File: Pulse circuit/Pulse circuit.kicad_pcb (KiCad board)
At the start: 2 copper layers, 4 parts, among them U1 ESP32-DevKitC, U2 module_max30102, U3 module_max30102

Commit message: Updated with relative path
🎯
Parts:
- U1: value ESP32-DevKitC -> module_max30102; footprint PCM_Espressif:ESP32-DevKitC -> usini_sensors:module_max30102
- U3: value module_max30102 -> DOIT-ESP32-DEVKIT-V1; footprint usini_sensors:module_max30102 -> doi-esp32-devkit:ESP32-DOIT-DEVKIT
- moved U3 65.5 mm to (239.4, 57.5)
- moved U1 54.7 mm to (132.7, 103.6)
- moved U2 42.9 mm to (149.7, 103.6)
- moved Brd1 24.2 mm to (79.6, 85.2)

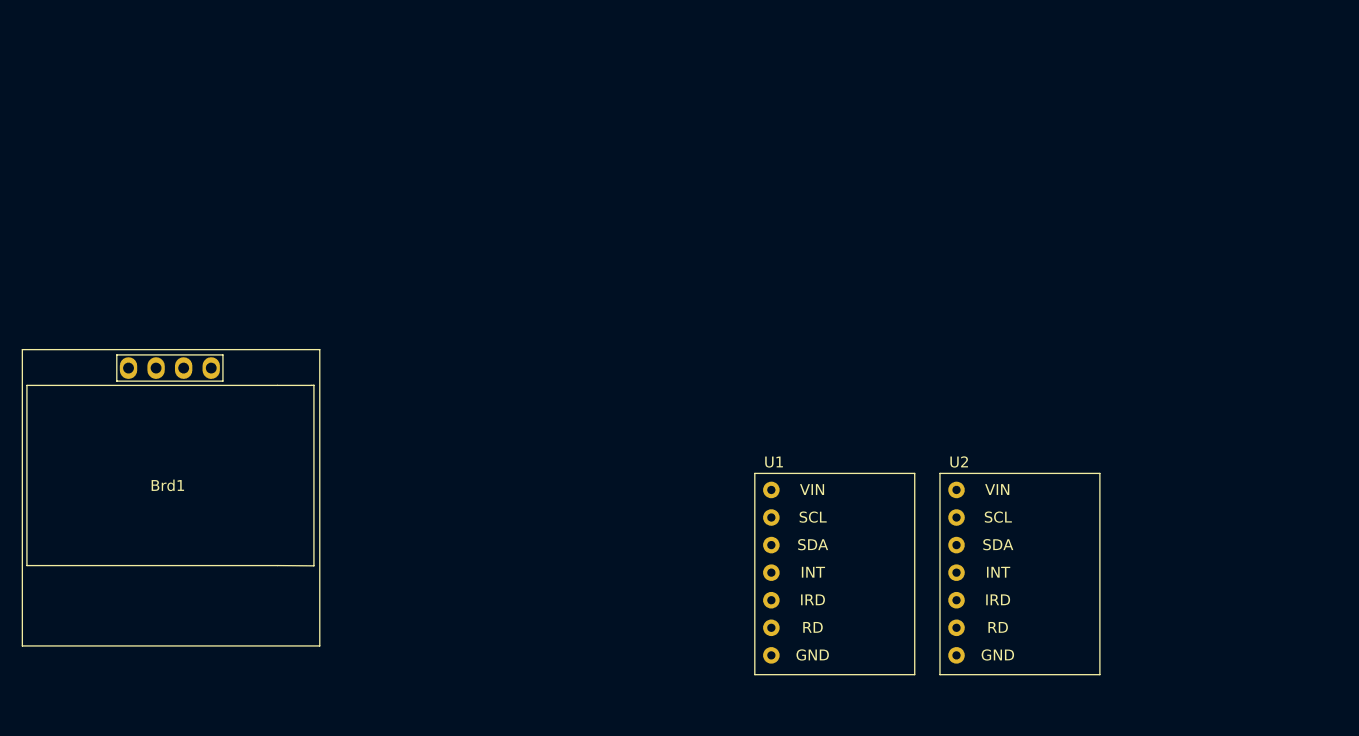
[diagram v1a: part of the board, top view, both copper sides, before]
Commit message: Changed footprint of the resistors
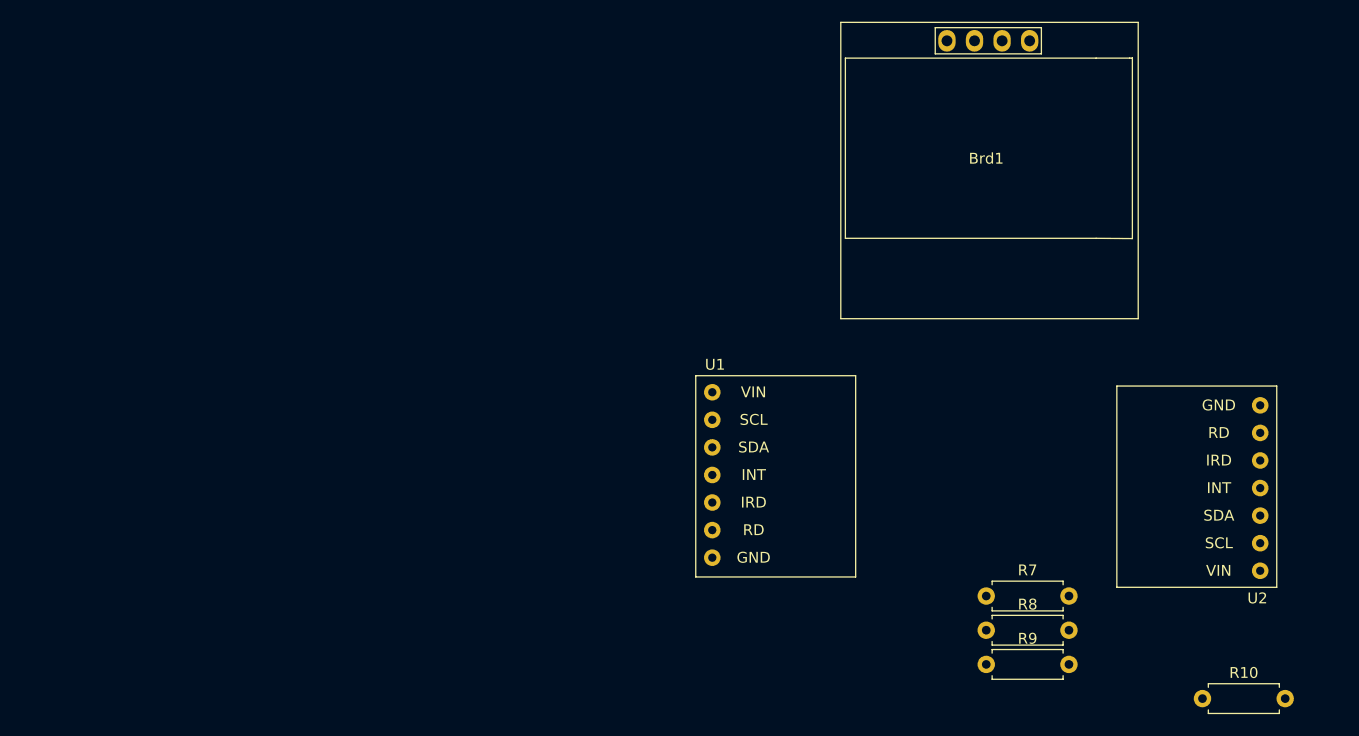
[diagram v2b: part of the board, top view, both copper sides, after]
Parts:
- added R10: 10k, Resistor_THT:R_Axial_DIN0207_L6.3mm_D2.5mm_P7.62mm_Horizontal, F.Cu at (174.9, 105.0)
- added R7: 10k, Resistor_THT:R_Axial_DIN0207_L6.3mm_D2.5mm_P7.62mm_Horizontal, F.Cu at (155.0, 95.5)
- added R8: 10k, Resistor_THT:R_Axial_DIN0207_L6.3mm_D2.5mm_P7.62mm_Horizontal, F.Cu at (155.0, 98.7)
- added R9: 10k, Resistor_THT:R_Axial_DIN0207_L6.3mm_D2.5mm_P7.62mm_Horizontal, F.Cu at (155.0, 101.8)
- moved Brd1 81.2 mm to (155.0, 55.0)
- moved U2 43.4 mm to (182.8, 75.4), turned to 180 degrees
- moved U1 10.5 mm to (127.2, 94.6)
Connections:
- Brd1 pad 1: unconnected-(Brd1-GND-Pad1) -> GND
- Brd1 pad 2: unconnected-(Brd1-VCC-Pad2) -> SDA
- Brd1 pad 3: unconnected-(Brd1-SCL-Pad3) -> SCL
- Brd1 pad 4: unconnected-(Brd1-SDA-Pad4) -> 3V3
- U1 pad 1: unconnected-(U1-VIN-Pad1) -> 3V3
- U1 pad 2: unconnected-(U1-SCL-Pad2) -> SCL
- U1 pad 3: unconnected-(U1-SDA-Pad3) -> SDA
- U1 pad 7: unconnected-(U1-GND-Pad7) -> GND
- U2 pad 1: unconnected-(U2-VIN-Pad1) -> 5V
- U2 pad 2: unconnected-(U2-SCL-Pad2) -> SCL
- U2 pad 3: unconnected-(U2-SDA-Pad3) -> SDA
- U2 pad 7: unconnected-(U2-GND-Pad7) -> GND
- U3 pad 18: unconnected-(U3-VIN-Pad18) -> 5V
- U3 pad 19: unconnected-(U3-3V3-Pad19) -> 3V3
- U3 pad 32: unconnected-(U3-GPIO21_I2C-SDA-Pad32) -> SDA
- U3 pad 35: unconnected-(U3-GPIO22_I2C-SCL-Pad35) -> SCL

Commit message: PCB 1/2
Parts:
- removed R10, R9: 10k, Resistor_THT:R_Axial_DIN0207_L6.3mm_D2.5mm_P7.62mm_Horizontal
- added R11: 10k, Resistor_THT:R_Axial_DIN0207_L6.3mm_D2.5mm_P7.62mm_Horizontal, F.Cu at (128.4, 69.3)
- added R12: 10k, Resistor_THT:R_Axial_DIN0207_L6.3mm_D2.5mm_P7.62mm_Horizontal, F.Cu at (132.4, 69.3)
- U1: moved to B.Cu
- moved U3 89.7 mm to (151.9, 77.3)
- moved R8 39.6 mm to (176.7, 65.6), turned to 180 degrees
- moved R7 33.9 mm to (176.7, 69.5), turned to 180 degrees
- moved U1 31.8 mm to (152.0, 74.7), turned to 180 degrees
- moved U2 23.0 mm to (166.6, 59.1)
- moved Brd1 5.99 mm to (151.8, 60.0)
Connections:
- U1 pad 1: 3V3 -> GND
- U1 pad 4: unconnected-(U1-INT-Pad4) -> 3V3
- U1 pad 5: unconnected-(U1-IRD-Pad5) -> GND
- U1 pad 6: unconnected-(U1-RD-Pad6) -> RD3v3
- U1 pad 7: GND -> IRD3v3
- U2 pad 4: unconnected-(U2-INT-Pad4) -> GND
- U2 pad 5: unconnected-(U2-IRD-Pad5) -> INT5v
- U2 pad 6: unconnected-(U2-RD-Pad6) -> IRD5v
- U2 pad 7: GND -> RD5v
- U3 pad 4: unconnected-(U3-GPIO34_ADC1-CH6_RTC-GPIO4-Pad4) -> RD3v3
- U3 pad 5: unconnected-(U3-GPIO35_ADC1-CH7_RTC-GPIO5-Pad5) -> IRD3v3
- U3 pad 6: unconnected-(U3-GPIO32_ADC1-CH4_RTC-GPIO9-Pad6) -> INT3v3
- U3 pad 7: unconnected-(U3-GPIO33_ADC1-CH5_RTC-GPIO8-Pad7) -> INT5v
- U3 pad 8: unconnected-(U3-GPIO25_ADC2-CH8_DAC1_RTC-GPIO6-Pad8) -> RD5v
- U3 pad 9: unconnected-(U3-GPIO26_ADC2-CH9_DAC2_RTC-GPIO7-Pad9) -> IRD5v
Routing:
- net SCL: track 0.00 -> 128.3 mm
- net SDA: track 0.00 -> 108.7 mm
- net IRD5v: track 0.00 -> 53.1 mm
- net RD5v: track 0.00 -> 42.0 mm
- net RD3v3: track 0.00 -> 31.3 mm
- net IRD3v3: track 0.00 -> 28.9 mm
- net INT3v3: track 0.00 -> 27.2 mm
- net INT5v: track 0.00 -> 18.1 mm
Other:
- copper layers 2 -> 4

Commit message: Added the GND plane
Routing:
- net GND: vias 0 -> 4
- added copper zone on In2.Cu, net GND
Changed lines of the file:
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@@
 			(layer "F.SilkS")
+		)
+		(fp_text user "GND"
+			(at 9.775 -10.03 0)
+			(layer "B.SilkS")
+			(effects
+				(font
+					(size 1 1)
+					(thickness 0.15)
+				)
+				(justify mirror)
+			)
 		)
 		(fp_text user "SCL"
@@
 			)
 		)
-		(fp_text user "GND"
-			(at 9.775 -10.03 0)
+		(fp_text user "RD"
+			(at 9.775 -7.49 0)
+			(layer "B.SilkS")
+			(effects
+				(font
+					(size 1 1)
+					(thickness 0.15)
+				)
+				(justify mirror)
+			)
+		)
+		(fp_text user "SDA"
+			(at 5.65 -7.515 0)
+			(layer "B.SilkS")
+			(effects
+				(font
+					(size 1 1)
+					(thickness 0.15)
+				)
+				(justify mirror)
+			)
+		)
+		(fp_text user "IRD"
+			(at 9.775 -4.95 0)
+			(layer "B.SilkS")
+			(effects
+				(font
+					(size 1 1)
+					(thickness 0.15)
+				)
+				(justify mirror)
+			)
+		)
+		(fp_text user "VIN"
+			(at 5.65 -10.055 0)
 			(layer "B.SilkS")
 			(effects
@@
 		(fp_text user "INT"
 			(at 9.775 -2.41 0)
-			(layer "B.SilkS")
-			(effects
-				(font
-					(size 1 1)
-					(thickness 0.15)
-				)
-				(justify mirror)
-			)
-		)
-		(fp_text user "RD"
-			(at 9.775 -7.49 0)
-			(layer "B.SilkS")
-			(effects
-				(font
-					(size 1 1)
-					(thickness 0.15)
-				)
-				(justify mirror)
-			)
-		)
-		(fp_text user "SDA"
-			(at 5.65 -7.515 0)
-			(layer "B.SilkS")
-			(effects
-				(font
-					(size 1 1)
-					(thickness 0.15)
-				)
-				(justify mirror)
-			)
-		)
-		(fp_text user "IRD"
-			(at 9.775 -4.95 0)
-			(layer "B.SilkS")
-			(effects
-				(font
-					(size 1 1)
-					(thickness 0.15)
-				)
-				(justify mirror)
-			)
-		)
-		(fp_text user "VIN"
-			(at 5.65 -10.055 0)
 			(layer "B.SilkS")
 			(effects
@@
 		(net 3)
 	)
+	(via
+		(at 138.344606 69.1675)
+		(size 0.6)
+		(drill 0.3)
+		(layers "F.Cu" "B.Cu")
+		(net 4)
+	)
+	(via
+		(at 164.0325 61.61)
+		(size 0.6)
+		(drill 0.3)
+		(layers "F.Cu" "B.Cu")
+		(net 4)
+	)
+	(via
+		(at 154.0325 69.23)
+		(size 0.6)
+		(drill 0.3)
+		(layers "F.Cu" "B.Cu")
+		(net 4)
+	)
+	(via
+		(at 148.344606 61.5475)
+		(size 0.6)
+		(drill 0.3)
+		(layers "F.Cu" "B.Cu")
+		(net 4)
+	)
 	(segment
 		(start 148.344606 83.475394)
@@
 		(net 11)
 	)
+	(zone
+		(net 4)
+		(net_name "GND")
+		(layer "In2.Cu")
+		(hatch edge 0.5)
+		(connect_pads
+			(clearance 0.5)
+		)
+		(min_thickness 0.25)
+		(filled_areas_thickness no)
+		(fill yes
+			(thermal_gap 0.5)
+			(thermal_bridge_width 0.5)
+		)
+		(polygon
+			(pts
+				(xy 124.67 44.17) (xy 178.62 44.61) (xy 180.82 125.25) (xy 123.35 127.16)
+			)
+		)
+	)
 	(group ""

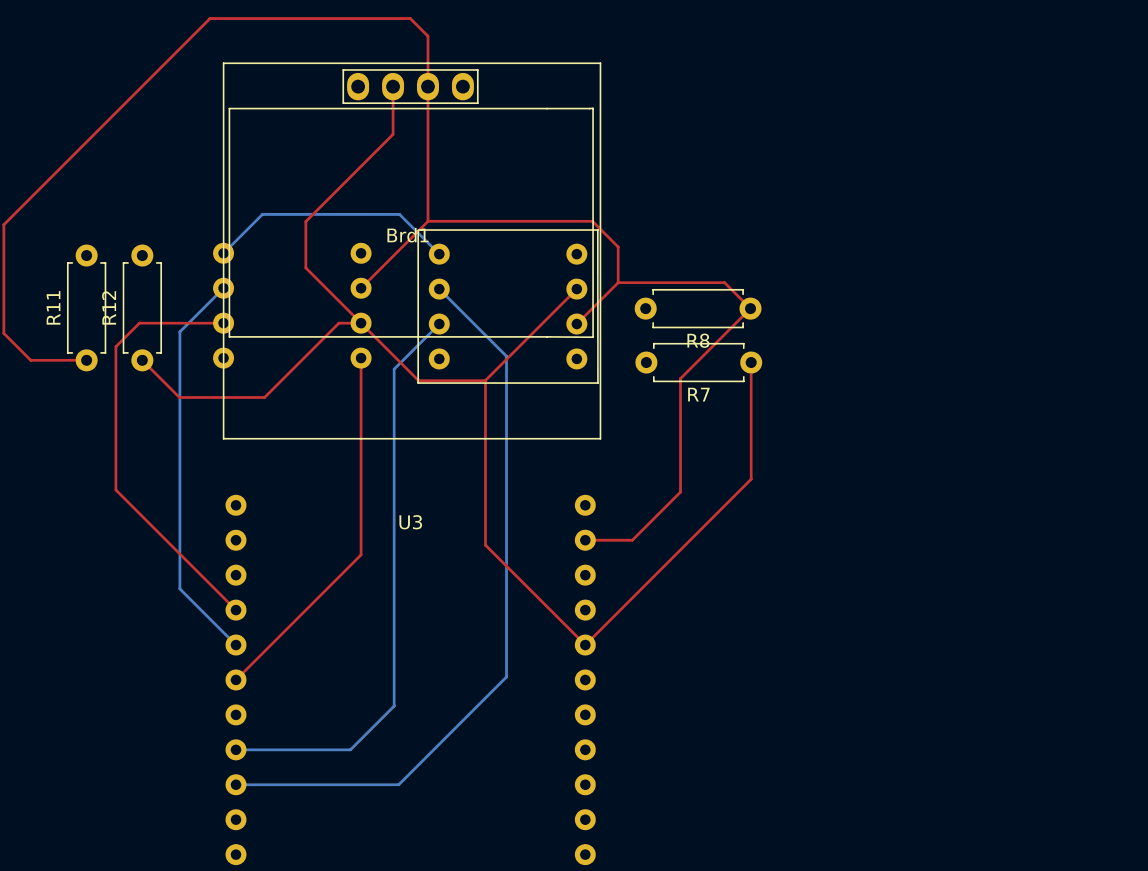
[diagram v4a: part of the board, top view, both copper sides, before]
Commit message: Added the power plane
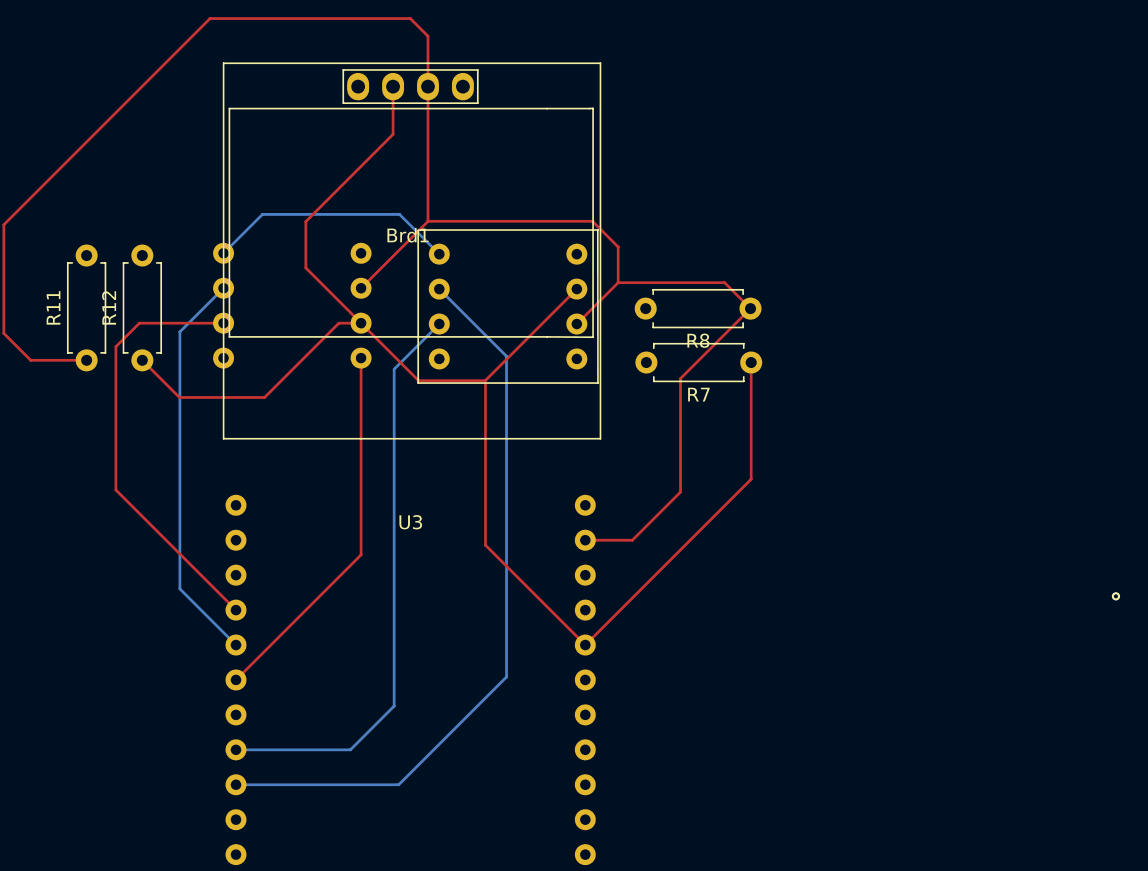
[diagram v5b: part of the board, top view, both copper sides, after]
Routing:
- net RD5v: vias 0 -> 2
- net RD3v3: vias 0 -> 2
- net IRD5v: vias 0 -> 2
- net IRD3v3: vias 0 -> 2
- net INT5v: vias 0 -> 2
- net INT3v3: vias 0 -> 1
- net GND: vias 4 -> 5
- net 5V: vias 0 -> 3
- net 3V3: vias 0 -> 3
- net (no net): vias 0 -> 1
- added copper zone on In1.Cu, net 3V3
- added copper zone on In1.Cu, net 5V

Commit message: Made some changes
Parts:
- U1: moved to F.Cu
- moved U1 15.3 mm to (136.7, 74.7), turned to 0 degrees
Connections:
- U1 pad 8: INT5v -> INT3v3
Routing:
- net 5V: track 0.00 -> 73.2 mm, vias 3 -> 0
- net INT5v: track 18.1 -> 41.1 mm, vias 2 -> 0
- net INT3v3: track 27.2 -> 34.5 mm, vias 1 -> 0
- net RD5v: vias 2 -> 1
- net RD3v3: vias 2 -> 0
- net IRD5v: vias 2 -> 1
- net IRD3v3: vias 2 -> 0
- net GND: vias 5 -> 0
- net 3V3: vias 3 -> 0
- net (no net): vias 1 -> 0
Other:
- board outline added: 76.9 x 88 mm

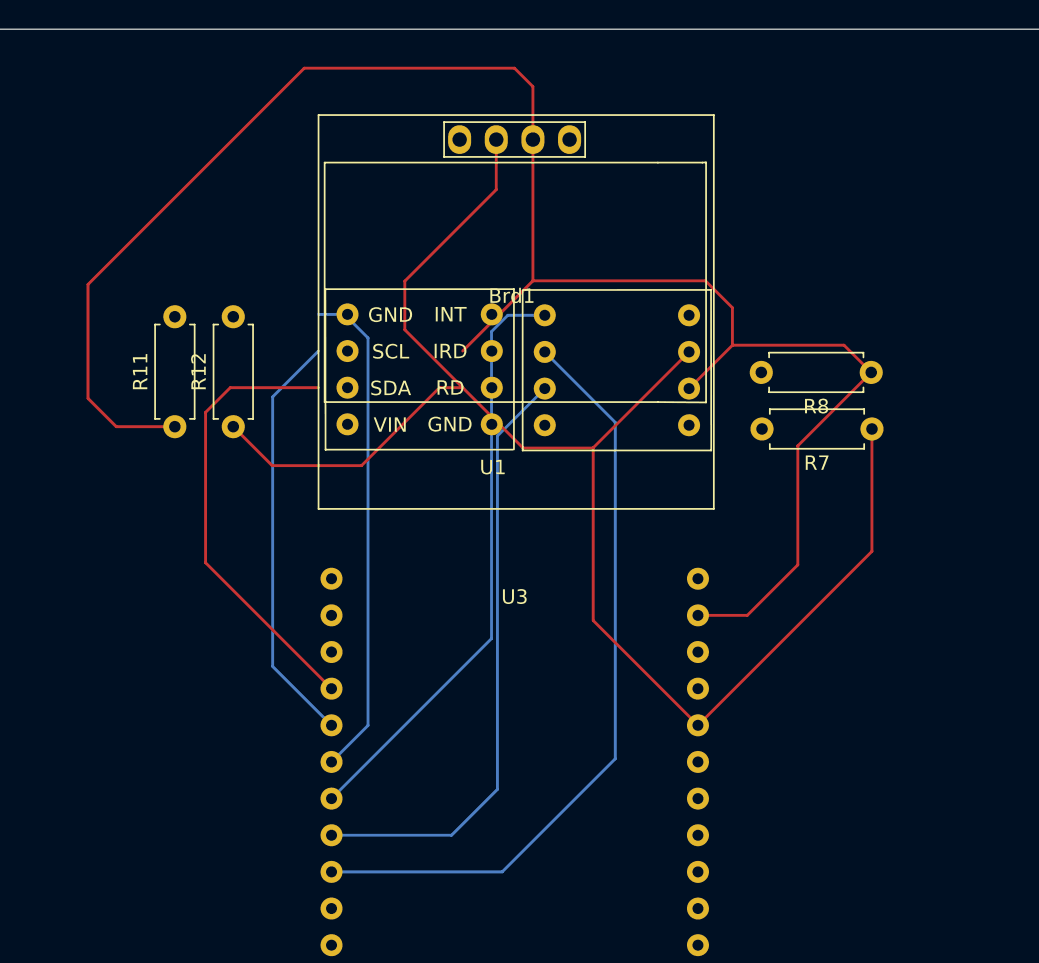
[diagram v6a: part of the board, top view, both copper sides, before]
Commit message: Rerouted the PCB
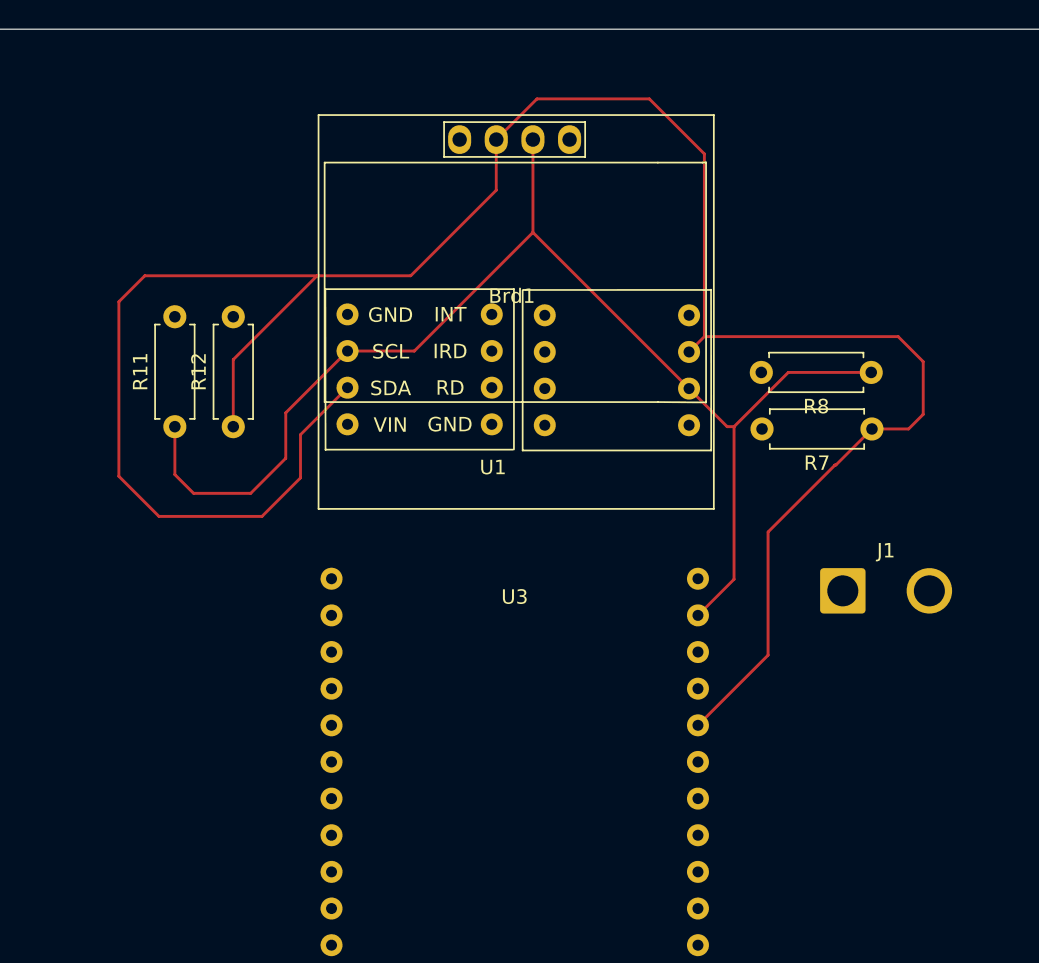
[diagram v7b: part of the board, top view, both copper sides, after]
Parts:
- added J1: Conn_01x02_Pin, Connector_Wire:SolderWire-1.5sqmm_1x02_P6mm_D1.7mm_OD3mm, F.Cu at (174.7, 80.7)
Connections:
- U1 pad 1: GND -> 3V3
- U1 pad 4: 3V3 -> INT3v3
- U1 pad 5: GND -> IRD3v3
- U1 pad 7: IRD3v3 -> GND
- U1 pad 8: INT3v3 -> (no net)
- U2 pad 4: GND -> INT5v
- U2 pad 5: INT5v -> IRD5v
- U2 pad 6: IRD5v -> RD5v
- U2 pad 7: RD5v -> GND
- U2 pad 8: GND -> (no net)
- U3 pad 12: unconnected-(U3-GPIO12_ADC2-CH5_HSPI-MISO_RTC-GPIO15-Pad12) -> B
- U3 pad 17: unconnected-(U3-GND-Pad17) -> GND
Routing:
- net IRD5v: track 53.1 -> 0.02 mm, vias 1 -> 0
- net SDA: track 108.7 -> 160.7 mm
- net RD5v: track 42.0 -> 0.00 mm, vias 1 -> 0
- net INT5v: track 41.1 -> 0.00 mm
- net SCL: track 128.3 -> 89.2 mm
- net INT3v3: track 34.5 -> 0.00 mm
- net RD3v3: track 31.3 -> 0.00 mm
- net IRD3v3: track 28.9 -> 0.00 mm
